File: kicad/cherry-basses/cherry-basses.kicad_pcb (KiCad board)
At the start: 2 copper layers, 175.4 x 53.4 mm, 42 parts, among them SW0 SPST, SW1.1 SPST, SW1.2 SPST, SW1.3 SPST, SW1.4 SPST, SW1.5 SPST, SW1.6 SPST, SW1.7 SPST, SW1.8 SPST, SW2.0 SPST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

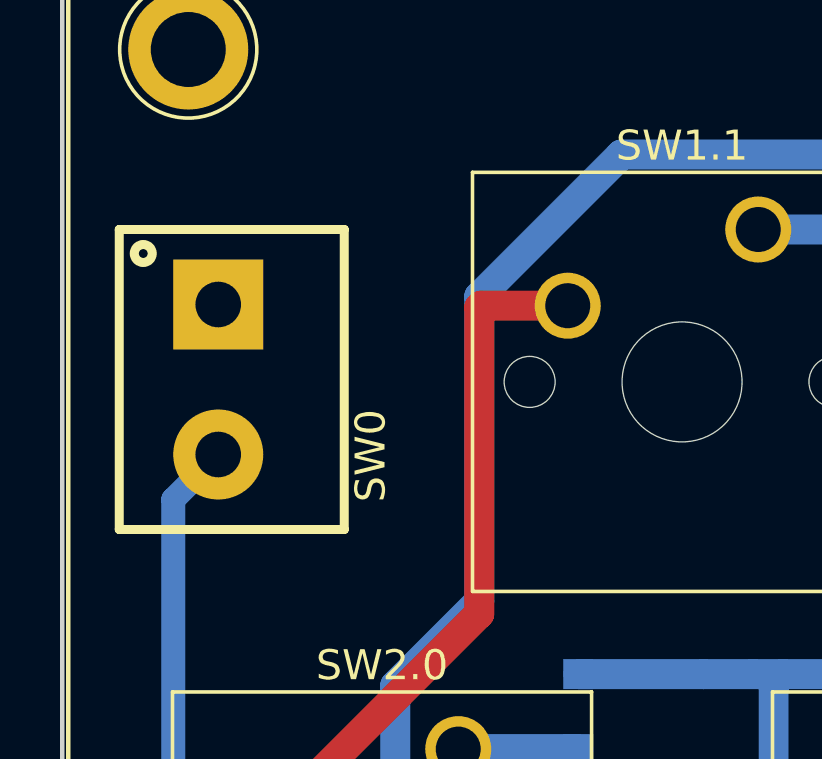
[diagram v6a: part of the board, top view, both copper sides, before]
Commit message: Move pushpull switch name on cherry basses
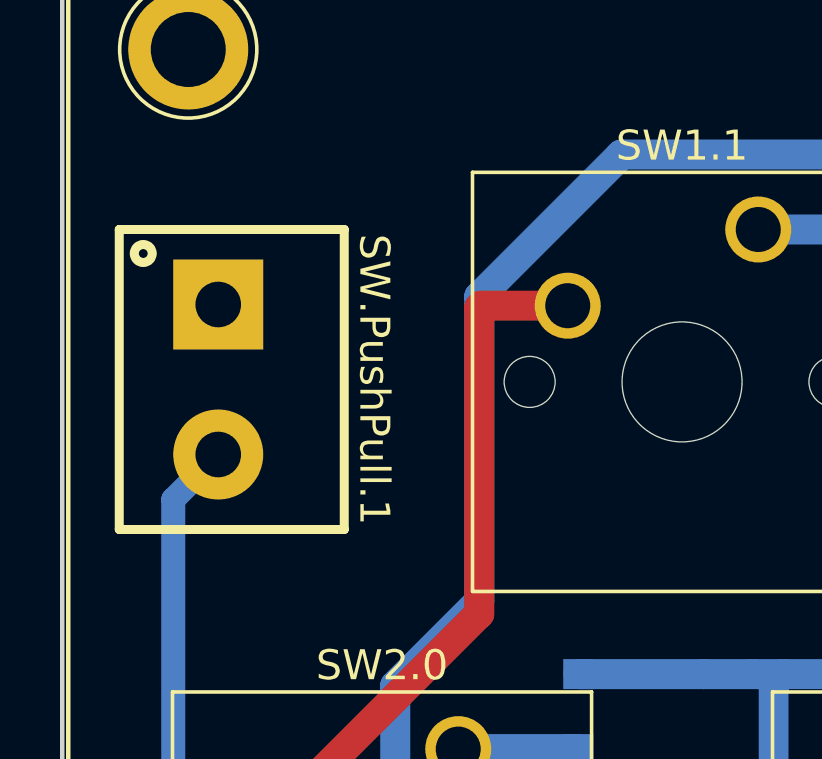
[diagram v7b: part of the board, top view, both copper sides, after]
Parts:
- renumbered SW0 to SW.PushPull.1
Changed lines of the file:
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@@
     (property "Sheetname" "")
     (attr through_hole)
-    (fp_text reference "SW0" (at 2.54 -5.08 90) (layer "F.SilkS")
+    (fp_text reference "SW.PushPull.1" (at 0 -5.2 -90 unlocked) (layer "F.SilkS")
       (effects (font (size 1 1) (thickness 0.15)))
     )

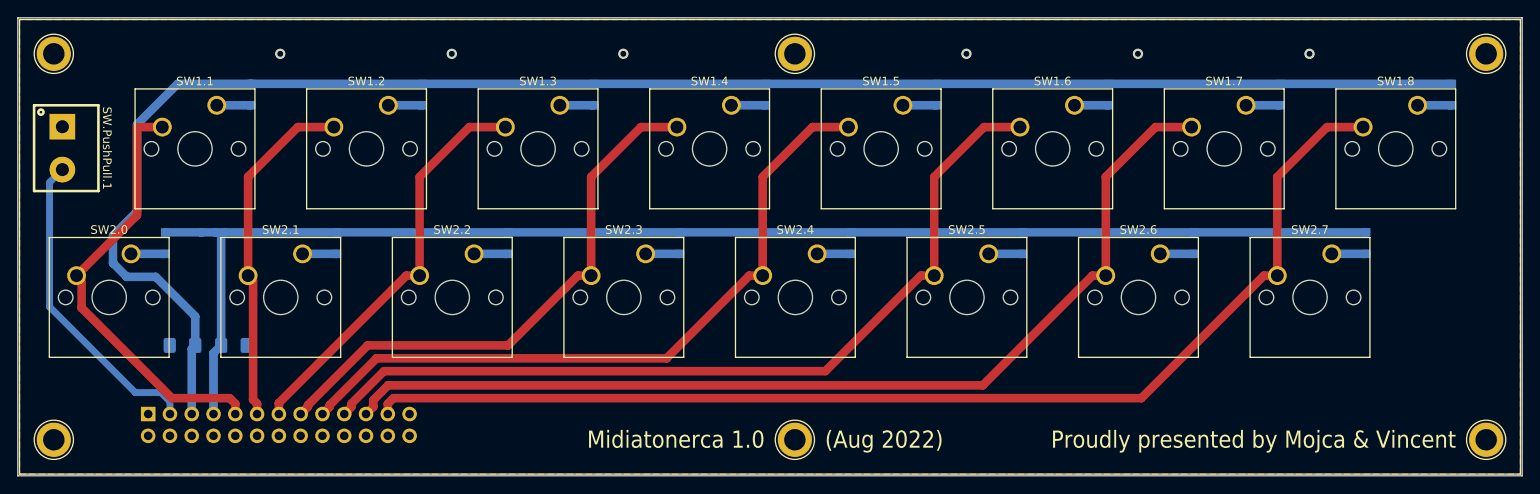
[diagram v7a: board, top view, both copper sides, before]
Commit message: cherry basses: replace components for rendering, add some vias
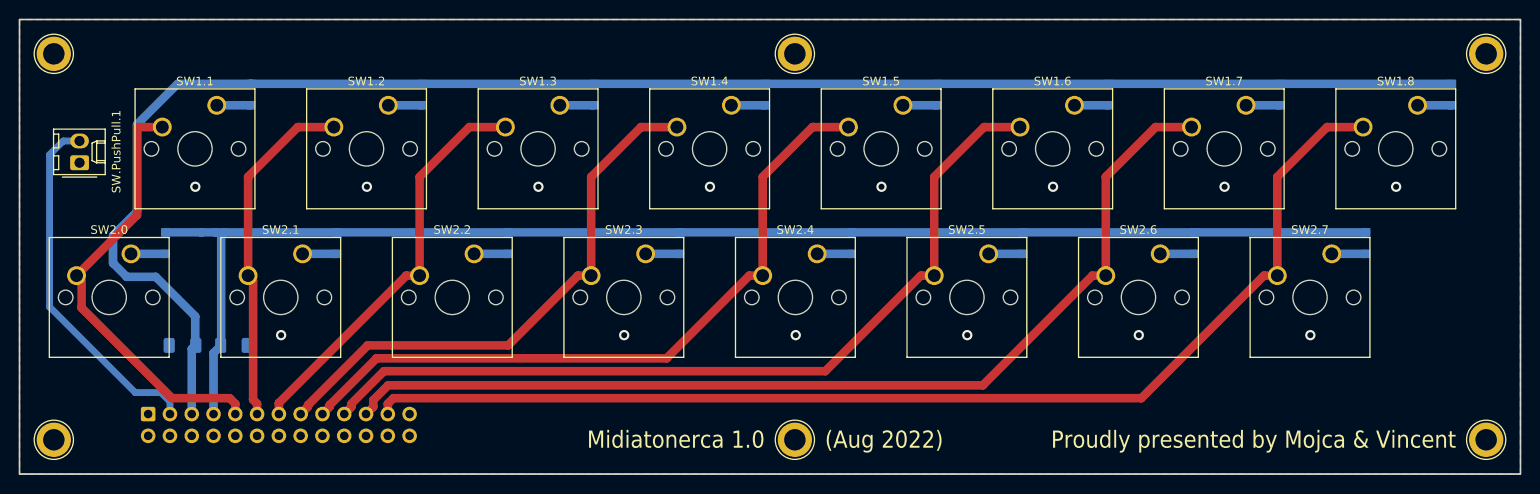
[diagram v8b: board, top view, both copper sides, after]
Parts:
- Conn1: footprint Connector_Multicomp:Multicomp_MC9A12-2634_2x13_P2.54mm_Vertical -> Connector_IDC:IDC-Header_2x13_P2.54mm_Vertical
- R1, R2: footprint Resistor_SMD:R_1206_3216Metric_Pad1.42x1.75mm_HandSolder -> Resistor_SMD:R_1206_3216Metric_Pad1.30x1.75mm_HandSolder
- SW.PushPull.1: footprint Library:Neltron-5523S-XX-10-X-Terminal-P5.0mm-7.5x10 -> Connector_Molex:Molex_KK-254_AE-6410-02A_1x02_P2.54mm_Vertical
- moved SW.PushPull.1 2.62 mm to (54.0, 56.7), turned to 90 degrees
- turned Conn1 to -90 degrees
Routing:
- net arduino_D2: track 36.7 -> 42.0 mm
- net GND: vias 6 -> 14
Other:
- board size 175.4 x 53.4 mm -> 175 x 53 mm
